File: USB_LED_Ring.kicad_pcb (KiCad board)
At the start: 2 copper layers, 91.6 x 75.1 mm, 84 parts, among them J1 .100, J2 USB_B_Micro, J3 JST SH 3 Vert, J4 JST SH 3 Vert, U1 TPS22917DBV, U2 TPS923610, U3 W25Q16JVUXIQ, U4 TLV75733PDBV, U5 RP2040, Y1 ABM8-272-T3

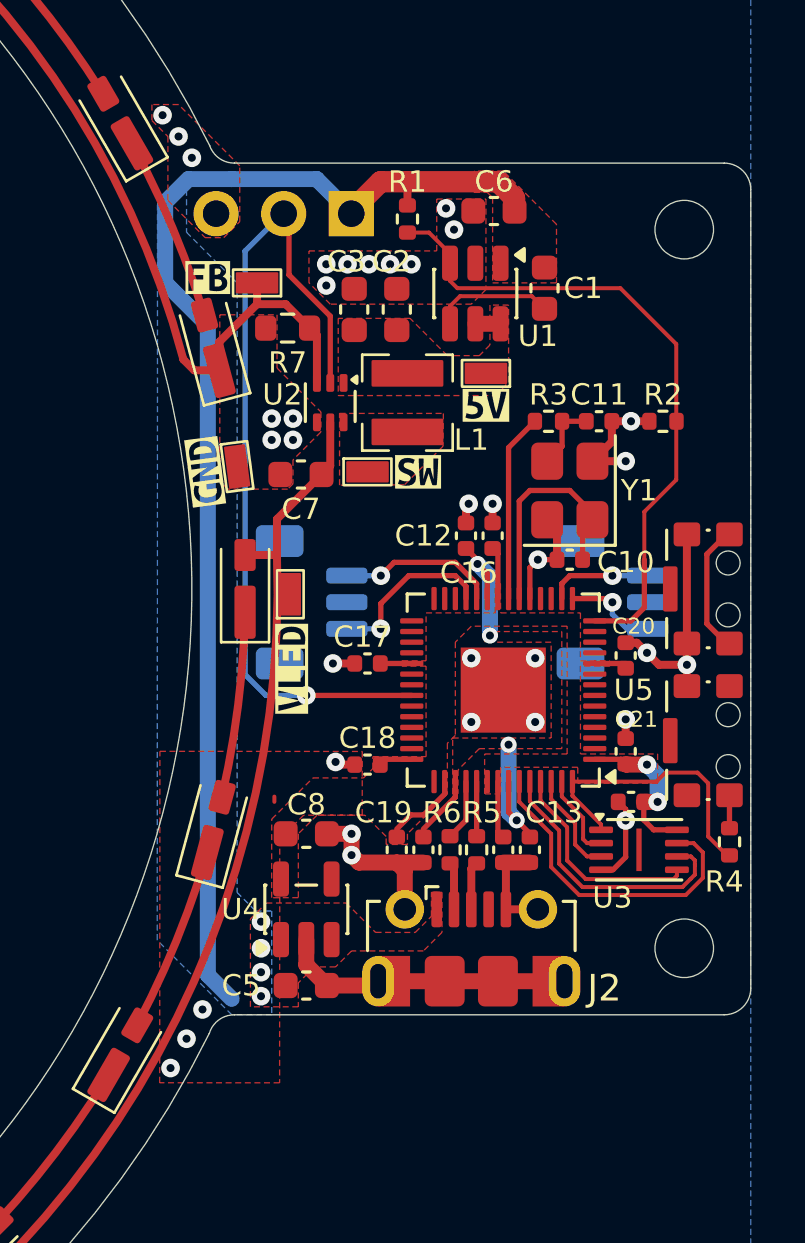
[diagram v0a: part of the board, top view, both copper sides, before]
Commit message: Uses RP2354A instead of RP2040 It simplifies the BOM a lot, and removes an hard to solder component
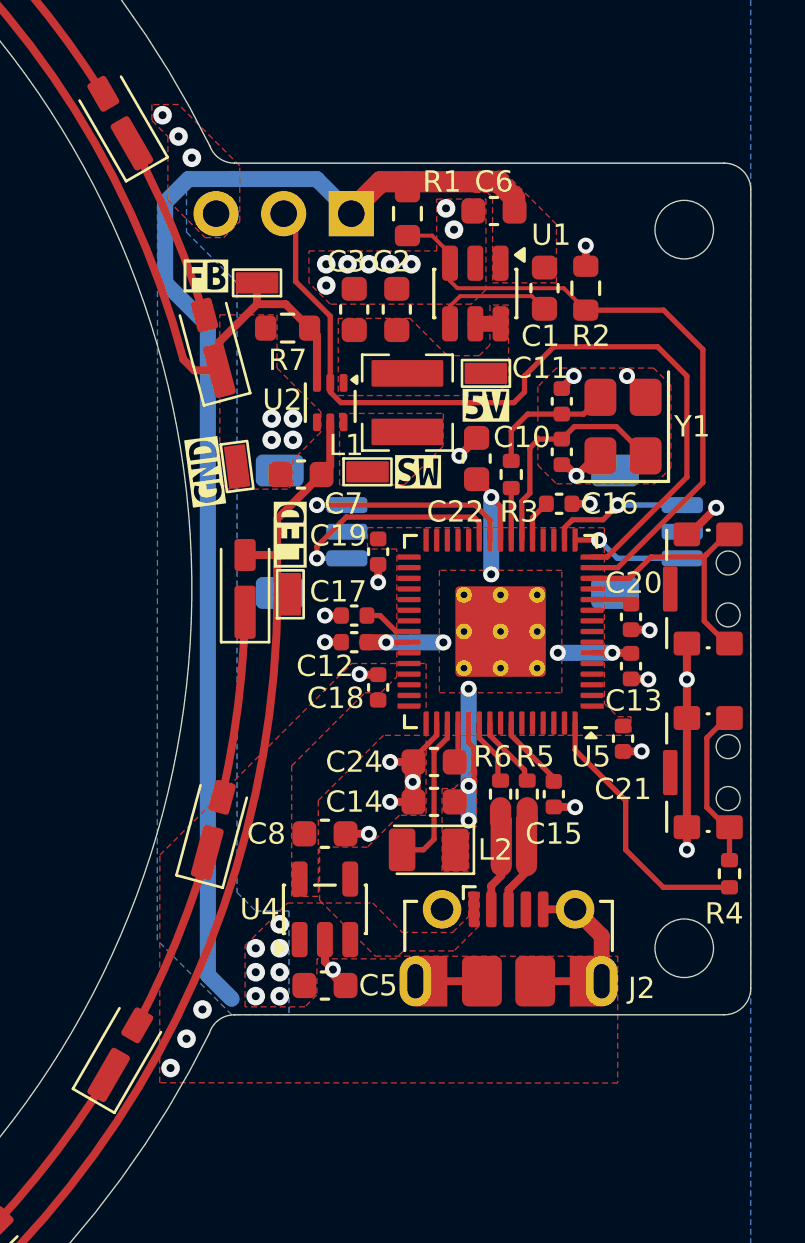
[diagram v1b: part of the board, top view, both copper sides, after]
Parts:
- removed C4: 100n, Capacitor_SMD:C_0402_1005Metric
- removed U3: W25Q16JVUXIQ, Package_SON:Winbond_USON-8-1EP_3x2mm_P0.5mm_EP0.2x1.6mm
- removed kibuzzard-69FB666A: G***, kibuzzard-69FB666A
- added C22: 4u7, Capacitor_SMD:C_0603_1608Metric, F.Cu at (193.7, 95.1)
- added C24: 4u7, Capacitor_SMD:C_0603_1608Metric, F.Cu at (192.1, 106.5)
- added L2: 3u3, custom:L_Abracon_AOTA, F.Cu at (191.9, 109.8)
- added kibuzzard-6A01CBA8: G***, kibuzzard-6A01CBA8, F.Cu at (186.7, 98.0)
- C14: value 2u2 -> 4u7; footprint Capacitor_SMD:C_0402_1005Metric -> Capacitor_SMD:C_0603_1608Metric
- C19: value 2u2 -> 100n
- R1, R2: footprint Resistor_SMD:R_0402_1005Metric -> Resistor_SMD:R_0603_1608Metric
- REF**: value OSHW-Logo2_14.6x12mm_SilkScreen -> OSHW-Logo2_9.8x8mm_SilkScreen; footprint Symbol:OSHW-Logo2_14.6x12mm_SilkScreen -> Symbol:OSHW-Logo2_9.8x8mm_SilkScreen
- TP1, TP2, TP3, TP4, TP5: value 5019 -> RCUCTE
- U5: value RP2040 -> RP2354A; footprint Package_DFN_QFN:QFN-56-1EP_7x7mm_P0.4mm_EP3.2x3.2mm -> custom:RP2350-QFN-60-1EP_7x7_P0.4mm_EP3.4x3.4mm_ThermalVias
- moved C19 11.2 mm to (190.0, 98.6)
- moved C13 7.88 mm to (199.5, 102.9)
- moved C12 5.80 mm to (189.1, 102.0), turned to 180 degrees
- moved R2 5.78 mm to (197.8, 88.7), turned to 90 degrees
- moved C10 4.06 mm to (196.9, 94.8), turned to -90 degrees
- moved Y1 3.12 mm to (199.2, 93.9)
- moved J4 2.95 mm to (200.1, 97.8)
- moved C18 2.93 mm to (190.0, 103.7), turned to 90 degrees
- moved kibuzzard-69FC8383 2.87 mm to (184.5, 97.6)
- moved C15 2.82 mm to (196.6, 107.7)
- moved R5 2.82 mm to (195.6, 107.7)
- moved R6 2.82 mm to (194.6, 107.7)
- moved kibuzzard-69FC837B 2.80 mm to (196.5, 97.8)
- moved C16 2.77 mm to (196.8, 96.8), turned to 0 degrees
- moved J3 2.65 mm to (187.5, 97.8)
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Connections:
- J3 pad MP: (no net) -> GND
- J4 pad MP: (no net) -> GND
- U5 pad 10: +3V3 -> unconnected-(U5-GPIO7-Pad10)
- U5 pad 11: unconnected-(U5-GPIO8-Pad11) -> +3V3
- U5 pad 13: unconnected-(U5-GPIO10-Pad13) -> /BTN
- U5 pad 15: /UART_TX -> /LED_PWM
- U5 pad 16: /UART_RX -> /UART_TX
- U5 pad 17: unconnected-(U5-GPIO14-Pad17) -> /UART_RX
- U5 pad 19: GND -> unconnected-(U5-GPIO15-Pad19)
- U5 pad 20: /XIN -> +3V3
- U5 pad 21: /XOUT -> /XIN
- U5 pad 22: +3V3 -> /XOUT
- U5 pad 26: /RUN -> unconnected-(U5-RUN-Pad26)
- U5 pad 30: unconnected-(U5-GPIO19-Pad30) -> +3V3
- U5 pad 33: +3V3 -> unconnected-(U5-GPIO21-Pad33)
- U5 pad 36: /LED_PWM -> unconnected-(U5-GPIO24-Pad36)
- U5 pad 38: unconnected-(U5-GPIO26_ADC0-Pad38) -> +3V3
- U5 pad 39: unconnected-(U5-GPIO27_ADC1-Pad39) -> +1V1
- U5 pad 42: +3V3 -> unconnected-(U5-GPIO28_ADC2-Pad42)
- U5 pad 45: +1V1 -> +3V3
- U5 pad 46: /USB_DN -> +3V3
- U5 pad 47: /USB_DP -> GND
- U5 pad 48: +3V3 -> /VREG_FB
- U5 pad 51: /QSPI_IO3 -> /USB_DN
- U5 pad 52: /QSPI_SCLK -> /USB_DP
- U5 pad 53: /QSPI_IO0 -> +3V3
- U5 pad 54: /QSPI_IO2 -> +3V3
- U5 pad 55: /QSPI_IO1 -> unconnected-(U5-QSPI_SD3-Pad55)
- U5 pad 56: /QSPI_SS -> unconnected-(U5-QSPI_SCLK-Pad56)
- U5 pad 57: GND -> unconnected-(U5-QSPI_SD0-Pad57)
- U5 pad 6: unconnected-(U5-GPIO4-Pad6) -> +1V1
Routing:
- net /QSPI_IO3: track 12.2 -> 0.00 mm
- net /QSPI_SCLK: track 10.5 -> 0.00 mm
- net /QSPI_IO0: track 8.07 -> 0.00 mm
- net +3V3: track 16.8 -> 9.27 mm, vias 2 -> 0
- net +1V1: track 12.8 -> 20.2 mm, vias 4 -> 9
- net GND: track 45.5 -> 38.2 mm, vias 35 -> 40
- net /VREG_FB: track 0.00 -> 5.94 mm
- net /XOUT: track 7.07 -> 1.95 mm
- net /BTSL: track 1.24 -> 6.17 mm
- net /BTN: track 4.93 -> 9.70 mm
- net /QSPI_IO2: track 3.90 -> 0.00 mm
- net /QSPI_IO1: track 3.23 -> 0.00 mm
- net /SWCLK: track 5.97 -> 8.61 mm
- net /SWDIO: track 6.49 -> 8.88 mm
- net /XOUT_NP: track 2.64 -> 5.01 mm
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
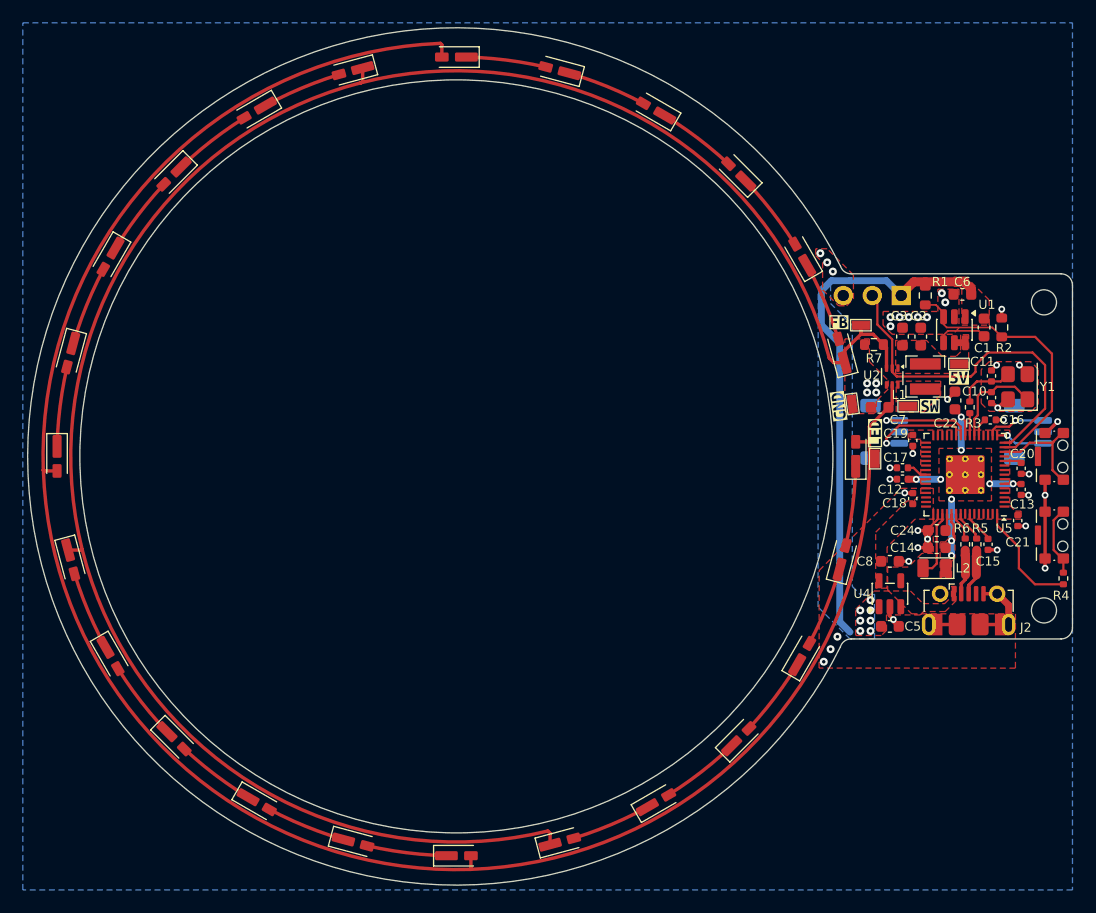
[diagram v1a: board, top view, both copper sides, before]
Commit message: Uses a Ferrite bead for Power Line Filtering.
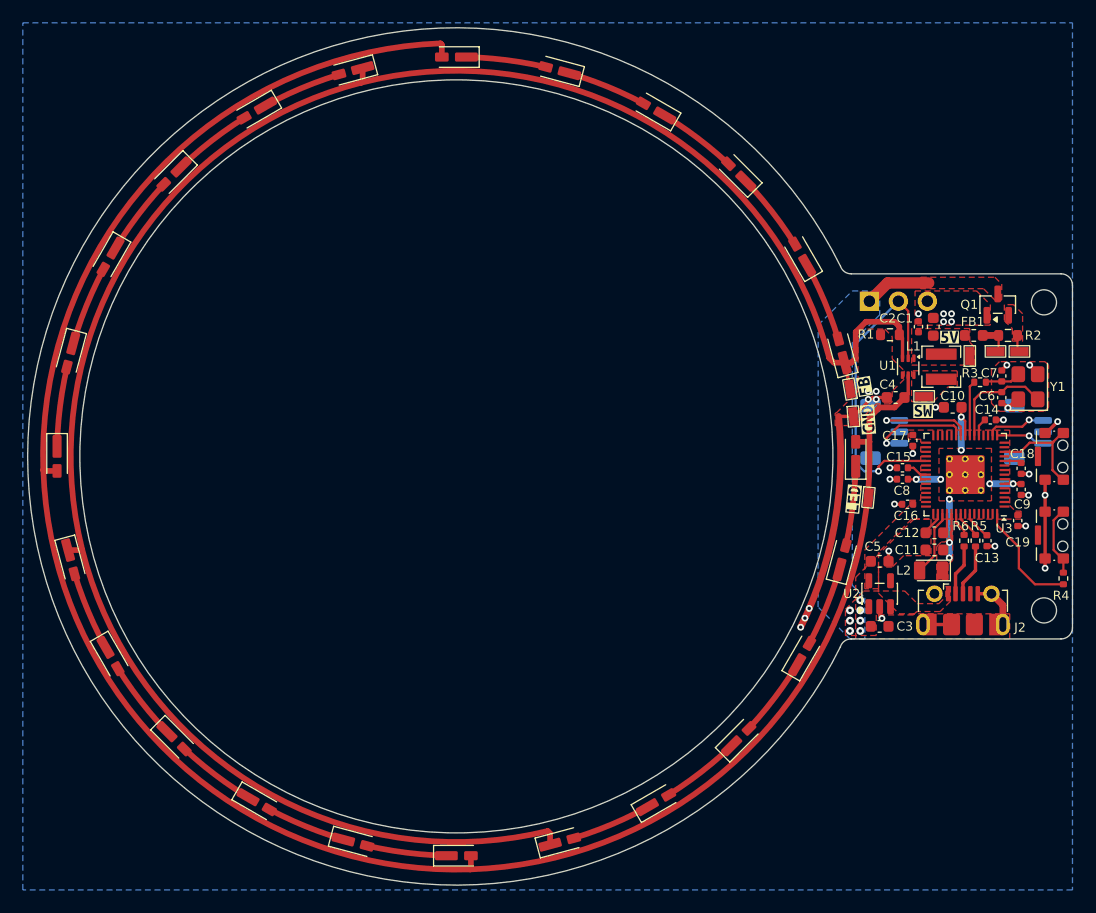
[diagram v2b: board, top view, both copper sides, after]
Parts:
- removed the C1 at (196.2, 88.7)
- removed the C6 at (194.3, 85.8)
- removed the R2 at (197.8, 88.7)
- removed the REF** at (196.7, 90.2)
- removed the TP1 at (194.1, 91.9)
- removed the TP4 at (186.7, 100.2)
- removed the U1 at (193.7, 88.9)
- removed kibuzzard-69FB6654: G***, kibuzzard-69FB6654
- added FB1: MPZ1608S601A, Inductor_SMD:L_0603_1608Metric, F.Cu at (195.3, 89.4)
- added Q1: DMG2305UX, Package_TO_SOT_SMD:SOT-23, F.Cu at (197.4, 86.7)
- added TP2: RCUCTE, custom:RCUCTE, F.Cu at (186.1, 103.6)
- added TP5: RCUCTE, custom:RCUCTE, F.Cu at (197.2, 90.8)
- added TP6: RCUCTE, custom:RCUCTE, F.Cu at (184.8, 96.5)
- added TP7: RCUCTE, custom:RCUCTE, F.Cu at (195.0, 91.2)
- added kibuzzard-6A0471EB: G***, kibuzzard-6A0471EB, F.Cu at (193.2, 89.6)
- C1: renamed from C2; value 10u -> 4u7
- C2: renamed from C3; value 10u -> 100n; footprint Capacitor_SMD:C_0603_1608Metric -> Capacitor_SMD:C_0402_1005Metric
- R2: renamed from R1; value 10k -> 250m
- moved TP4 15.4 mm to (199.3, 90.8), turned to 180 degrees
- moved R2 8.05 mm to (198.3, 89.4), turned to 180 degrees
- moved kibuzzard-69FB6788 7.38 mm to (191.3, 89.5)
- moved kibuzzard-6A01CBA8 6.08 mm to (184.8, 103.7), turned to 84.3 degrees
- moved kibuzzard-69FB66A2 6.06 mm to (185.8, 93.9), turned to 99.7 degrees
- moved TP3 5.68 mm to (184.5, 94.1), turned to 99.7 degrees
- moved J4 2.83 mm to (186.2, 86.4), turned to -90 degrees
- moved kibuzzard-69FB6681 2.83 mm to (186.1, 96.8), turned to 94 degrees
- moved kibuzzard-69FB6775 2.80 mm to (186.3, 89.9)
- moved R3 2.38 mm to (195.9, 93.5), turned to 0 degrees
- moved kibuzzard-69FB677C 2.33 mm to (188.7, 89.5)
- moved C2 1.64 mm to (190.5, 88.6)
- moved C4 1.64 mm to (188.5, 94.8)
- moved L1 1.64 mm to (192.5, 92.1)
- moved R1 1.64 mm to (188.0, 89.3)
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- renumbered C22 to C10, C14 to C11, C24 to C12, C15 to C13, C16 to C14, C17 to C15, C18 to C16, C19 to C17, C20 to C18, C21 to C19, C5 to C3, C7 to C4, C8 to C5, C10 to C6, C11 to C7, C12 to C8, C13 to C9, J3 to J1, J4 to J3, J1 to J4, R7 to R1, TP2 to TP1, TP5 to TP4, U2 to U1, U4 to U2, U5 to U3
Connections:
- R2 pad 1: VBUS -> Net-(Q1-S)
- R2 pad 2: /LED_RAIL_ON -> Net-(FB1-Pad2)
- TP4 pad 1: GND -> Net-(Q1-S)
- U3 pad 14: /LED_RAIL_ON -> unconnected-(U3-GPIO10-Pad14)
- U3 pad 15: /LED_PWM -> unconnected-(U3-GPIO11-Pad15)
- U3 pad 35: unconnected-(U5-GPIO23-Pad35) -> /LED_PWM
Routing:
- net VBUS: track 46.2 -> 5.86 mm
- net /LED_RAIL_ON: track 24.0 -> 0.00 mm
- net Net-(U1-CT): track 4.56 -> 0.00 mm
- net /LED_PWM: track 31.3 -> 28.1 mm, vias 0 -> 1
- net Net-(FB1-Pad2): track 0.00 -> 2.90 mm
- net /XOUT: track 1.95 -> 4.82 mm
- net GND: track 38.2 -> 35.4 mm, vias 40 -> 30
- net /LED_FB: track 13.8 -> 16.1 mm
- net /VLED: track 10.7 -> 12.9 mm
- net /XOUT_NP: track 5.01 -> 3.15 mm
- net Net-(Q1-S): track 0.00 -> 1.47 mm
- net +5V: track 0.99 -> 0.00 mm
- net /XIN: track 8.72 -> 9.62 mm
- added copper zone on F.Cu, net Net-(Q1-S)
